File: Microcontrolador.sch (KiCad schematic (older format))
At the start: 16 parts, among them U3 EFM32TG11B120F128GM32, Y1 Crystal, Y2 Crystal

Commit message: Issue #1: Correción de las conexiones Bus
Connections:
- net +3V3: now also C16.1, U3.20 (DVDD)
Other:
- note added: "Conexión UART0 (Location 5)\nU0_CTS: PD5\nU0_RTS: PD6\nU0_RX: PF2\nU0_TX: PF1\n\nComo configurar la funcionalidad de bootloader??\nSegún datasheet está en los pines PF0 y PF1:\nBOOT_RX: PF1\nBOOT_TX: PF0"
- note added: "Requerimientos de Tensión\n==================\n\nVREGVDD = AVDD (Debe ser el mayor volaje del sistema)\nAVDD >= DVDD\nAVDD >= IOVDD"
- note removed: "- PA0\nA: BUSBY BUSAX | LCD_SEG13 \nT: TIM0_CC0 #0 | TIM0_CC1 #7 | PCNT0_S0IN #4\nC: US1_RX #5 | US3_TX #0 | LEU0_RX #4 | I2C0_SDA #0\nO: CMU_CLK2 #0 | PRS_CH0 #0 | PRS_CH3 #3 | GPIO_EM4WU0\n\n- PA1\nA: BUSAY BUSBX | LCD_SEG14\nT: TIM0_CC0 #7 | TIM0_CC1 #0 | PCNT0_S1IN #4\nC: US3_RX #0 | I2C0_SCL #0\nO: CMU_CLK1 #0 PRS_CH1 #0\n\n- PA2\nA: BUSBY BUSAX | LCD_SEG15\nT: TIM0_CC2 #0\nC: US1_RX #6 | US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"
- note removed: "Conexión UART0 (Location 5)\nU0_CTS: PD5\nU0_RTS: PD6\nU0_RX: PF2\nU0_TX: PF1"
- note removed: "TABLA FUNCIONALIDAD GPIOs"
- moved on the sheet: C17, U3A

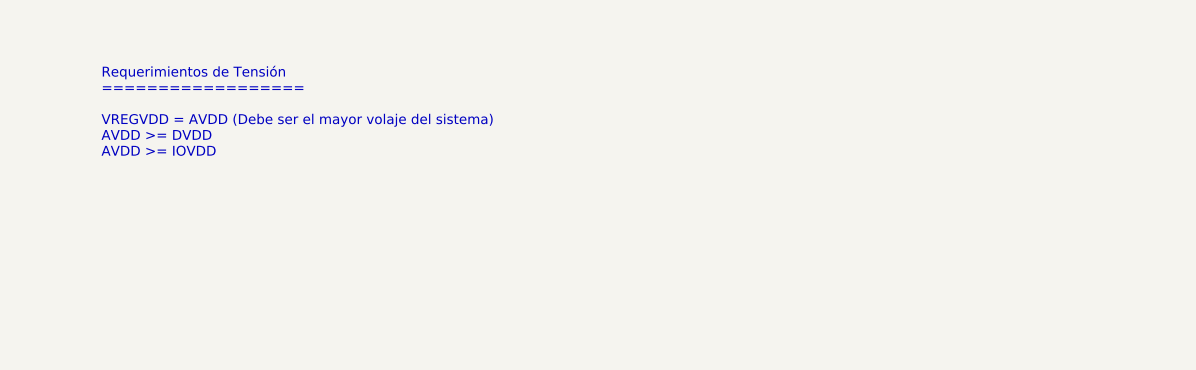
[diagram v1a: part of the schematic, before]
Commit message: Issue #1: Cambio de regulador de voltaje
Se reemplazó el MAX8887 de Maxim por el SP6260 de Maxlinear.
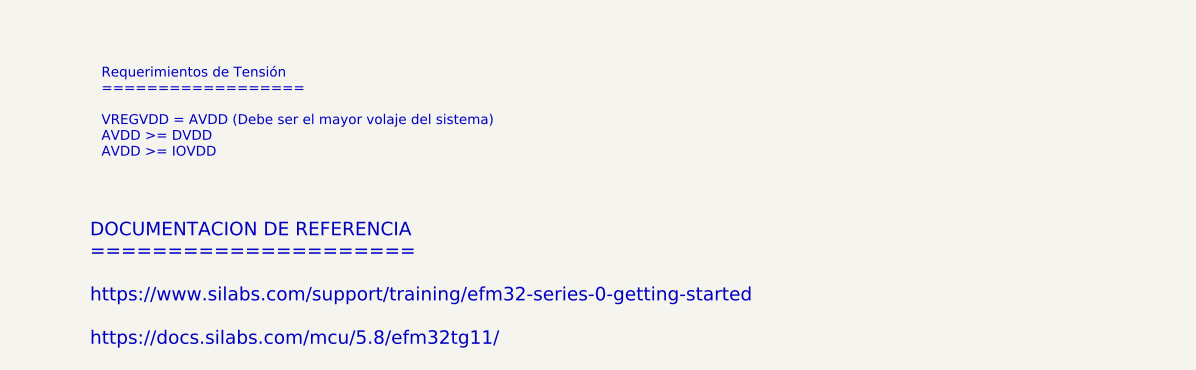
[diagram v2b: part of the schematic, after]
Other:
- note added: "DOCUMENTACION DE REFERENCIA\n=====================\n\nhttps://www.silabs.com/support/training/efm32-series-0-getting-started\n\nhttps://docs.silabs.com/mcu/5.8/efm32tg11/\n"
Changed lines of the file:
@@
 Wire Bus Line
 	6425 3525 6425 4425
+Text Notes 1500 6700 0    59   ~ 0
+DOCUMENTACION DE REFERENCIA\n=====================\n\nhttps://www.silabs.com/support/training/efm32-series-0-getting-started\n\nhttps://docs.silabs.com/mcu/5.8/efm32tg11/\n
 $EndSCHEMATC

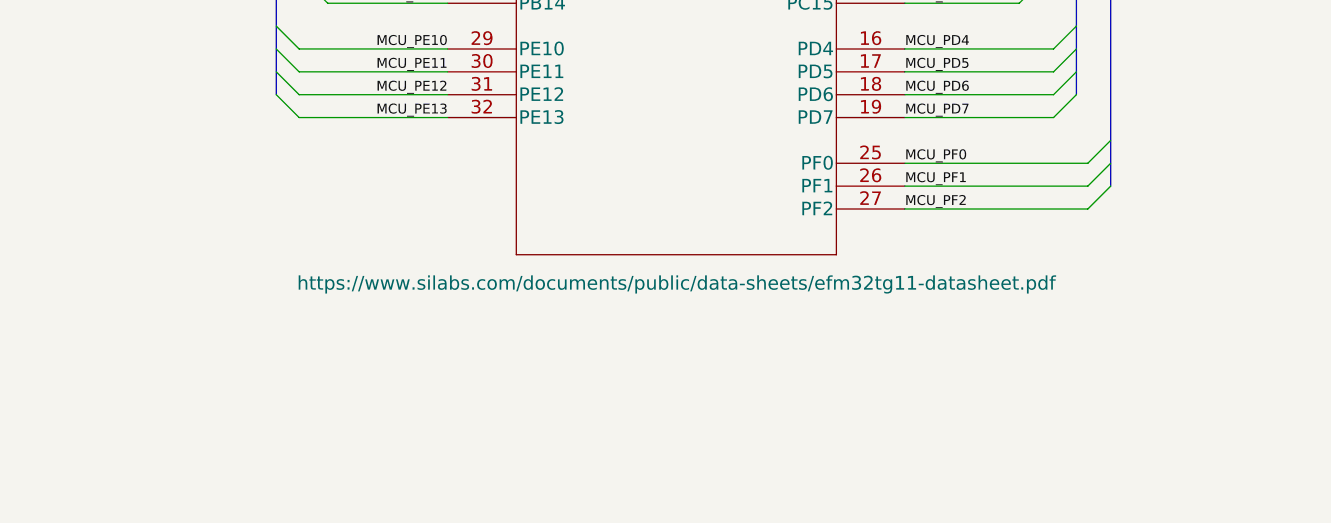
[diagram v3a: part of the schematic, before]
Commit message: Issue #1: Mejora de la funcionalidad de reset
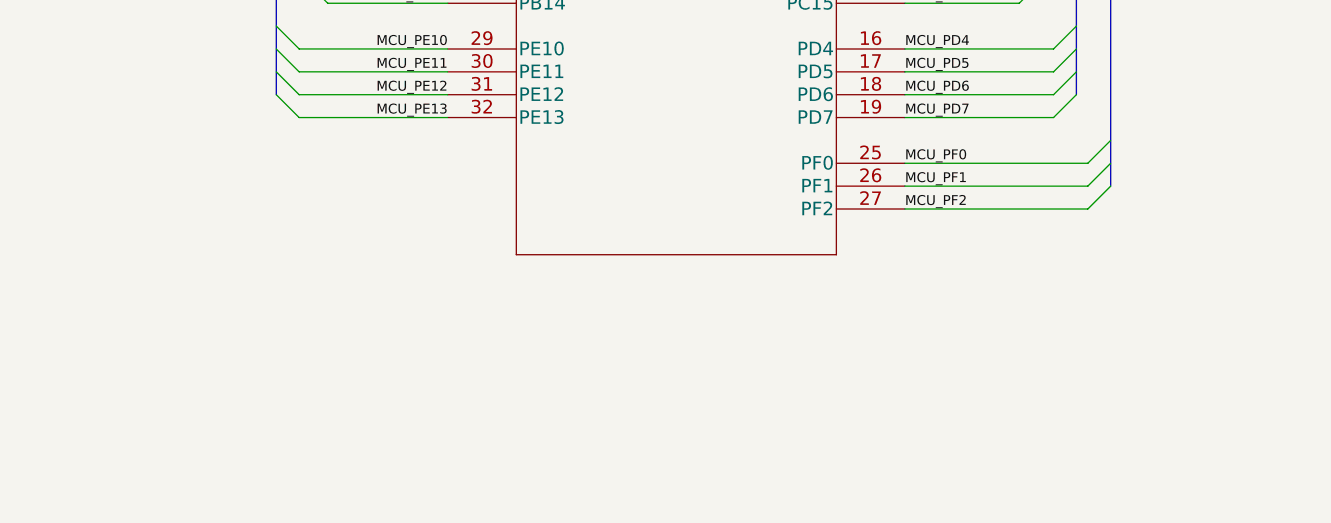
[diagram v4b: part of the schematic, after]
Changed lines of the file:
@@
 F 1 "EFM32TG11B120F128GM32" H 8050 3806 60  0000 C CNN
 F 2 "Mis Huellas:EFM32TG11B120F128GM32" H 8050 3765 60  0001 C CNN
-F 3 "https://www.silabs.com/documents/public/data-sheets/efm32tg11-datasheet.pdf" H 8050 1300 60  0000 C CNN
+F 3 "https://www.silabs.com/documents/public/data-sheets/efm32tg11-datasheet.pdf" H 8050 1300 60  0001 C CNN
 	1    7050 3525
 	1    0    0    -1

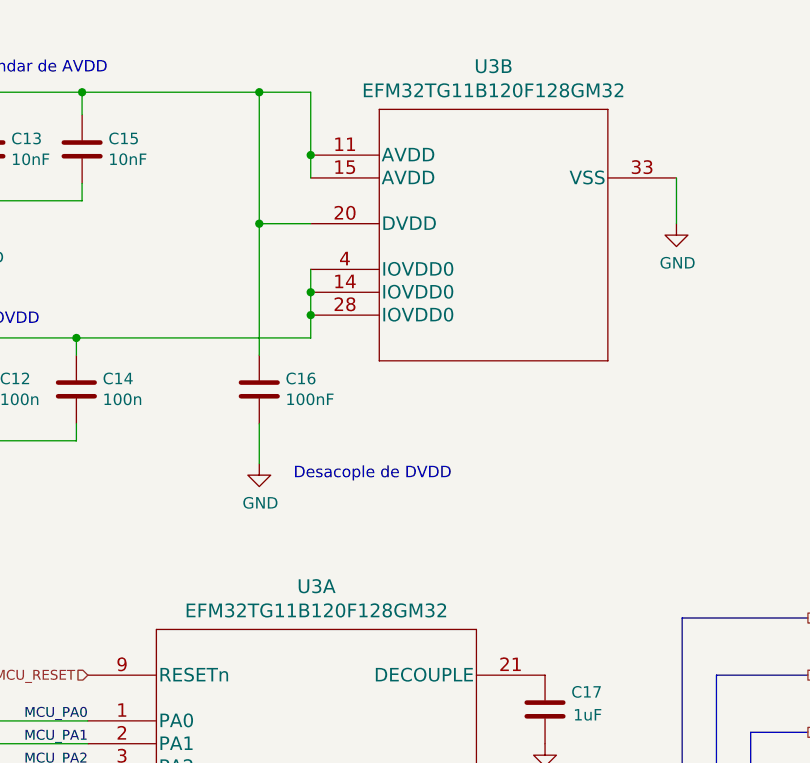
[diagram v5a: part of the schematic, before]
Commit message: Issue #1: Se agregan LEDs para líneas TX/RX de UART
Se agregan los LEDs para indicar comunicación vía UART. Se utilizó un
OpAmp para evitar un consumo excesivo de corriente en las líneas de
comunicación.

Referencia: https://bit.ly/2E7PuVE
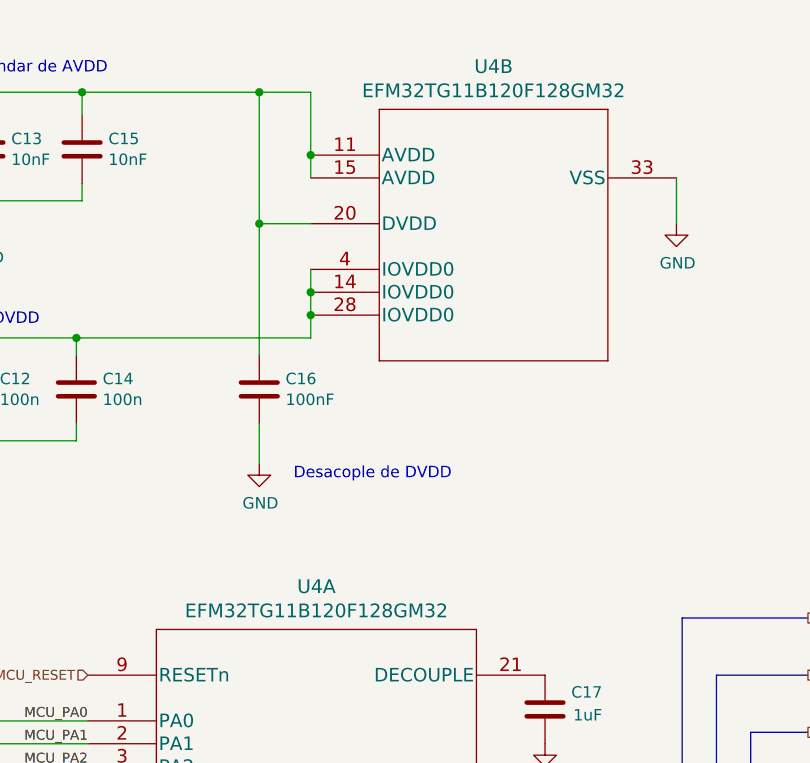
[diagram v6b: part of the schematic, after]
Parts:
- renumbered U3 to U4
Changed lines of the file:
@@
 P 7050 3525
 AR Path="/5F4D785E" Ref="U?"  Part="1"
-AR Path="/5F4D1FFB/5F4D785E" Ref="U3"  Part="1"
-F 0 "U3" H 8050 3912 60  0000 C CNN
+AR Path="/5F4D1FFB/5F4D785E" Ref="U4"  Part="1"
+F 0 "U4" H 8050 3912 60  0000 C CNN
 F 1 "EFM32TG11B120F128GM32" H 8050 3806 60  0000 C CNN
 F 2 "Mis Huellas:EFM32TG11B120F128GM32" H 8050 3765 60  0001 C CNN
@@
 P 8025 1250
 AR Path="/5F4D7864" Ref="U?"  Part="2"
-AR Path="/5F4D1FFB/5F4D7864" Ref="U3"  Part="2"
-F 0 "U3" H 8825 1637 60  0000 C CNN
+AR Path="/5F4D1FFB/5F4D7864" Ref="U4"  Part="2"
+F 0 "U4" H 8825 1637 60  0000 C CNN
 F 1 "EFM32TG11B120F128GM32" H 8825 1531 60  0000 C CNN
 F 2 "Mis Huellas:EFM32TG11B120F128GM32" H 9025 1490 60  0001 C CNN
@@
 P 9625 1550
 AR Path="/5F4D789A" Ref="#PWR?"  Part="1"
-AR Path="/5F4D1FFB/5F4D789A" Ref="#PWR034"  Part="1"
-F 0 "#PWR034" H 9625 1300 50  0001 C CNN
+AR Path="/5F4D1FFB/5F4D789A" Ref="#PWR038"  Part="1"
+F 0 "#PWR038" H 9625 1300 50  0001 C CNN
 F 1 "GND" H 9630 1377 50  0000 C CNN
 F 2 "" H 9625 1550 50  0001 C CNN
@@
 P 7800 2600
 AR Path="/5F4F6C62" Ref="#PWR?"  Part="1"
-AR Path="/5F4D1FFB/5F4F6C62" Ref="#PWR032"  Part="1"
-F 0 "#PWR032" H 7800 2350 50  0001 C CNN
+AR Path="/5F4D1FFB/5F4F6C62" Ref="#PWR036"  Part="1"
+F 0 "#PWR036" H 7800 2350 50  0001 C CNN
 F 1 "GND" H 7805 2427 50  0000 C CNN
 F 2 "" H 7800 2600 50  0001 C CNN
@@
 P 9050 3825
 AR Path="/5F50B022" Ref="#PWR?"  Part="1"
-AR Path="/5F4D1FFB/5F50B022" Ref="#PWR033"  Part="1"
-F 0 "#PWR033" H 9050 3575 50  0001 C CNN
+AR Path="/5F4D1FFB/5F50B022" Ref="#PWR037"  Part="1"
+F 0 "#PWR037" H 9050 3575 50  0001 C CNN
 F 1 "GND" H 9055 3652 50  0000 C CNN
 F 2 "" H 9050 3825 50  0001 C CNN
@@
 P 6600 1525
 AR Path="/5F50B78B" Ref="#PWR?"  Part="1"
-AR Path="/5F4D1FFB/5F50B78B" Ref="#PWR031"  Part="1"
-F 0 "#PWR031" H 6600 1275 50  0001 C CNN
+AR Path="/5F4D1FFB/5F50B78B" Ref="#PWR035"  Part="1"
+F 0 "#PWR035" H 6600 1275 50  0001 C CNN
 F 1 "GND" H 6605 1352 50  0000 C CNN
 F 2 "" H 6600 1525 50  0001 C CNN
@@
 P 2200 2050
 AR Path="/5F50B9C5" Ref="#PWR?"  Part="1"
-AR Path="/5F4D1FFB/5F50B9C5" Ref="#PWR025"  Part="1"
-F 0 "#PWR025" H 2200 1800 50  0001 C CNN
+AR Path="/5F4D1FFB/5F50B9C5" Ref="#PWR029"  Part="1"
+F 0 "#PWR029" H 2200 1800 50  0001 C CNN
 F 1 "GND" H 2205 1877 50  0000 C CNN
 F 2 "" H 2200 2050 50  0001 C CNN
@@
 P 6325 2600
 AR Path="/5F50B4BA" Ref="#PWR?"  Part="1"
-AR Path="/5F4D1FFB/5F50B4BA" Ref="#PWR030"  Part="1"
-F 0 "#PWR030" H 6325 2350 50  0001 C CNN
+AR Path="/5F4D1FFB/5F50B4BA" Ref="#PWR034"  Part="1"
+F 0 "#PWR034" H 6325 2350 50  0001 C CNN
 F 1 "GND" H 6330 2427 50  0000 C CNN
 F 2 "" H 6325 2600 50  0001 C CNN
@@
 	8025 1250 8025 1350
 $Comp
-L power:+3V3 #PWR029
+L power:+3V3 #PWR033
 U 1 1 5F52FE3B
 P 5900 875
-F 0 "#PWR029" H 5900 725 50  0001 C CNN
+F 0 "#PWR033" H 5900 725 50  0001 C CNN
 F 1 "+3V3" H 5915 1048 50  0000 C CNN
 F 2 "" H 5900 875 50  0001 C CNN
@@
 Connection ~ 6200 975
 $Comp
-L power:+3V3 #PWR028
+L power:+3V3 #PWR032
 U 1 1 5F531E0C
 P 5400 1875
-F 0 "#PWR028" H 5400 1725 50  0001 C CNN
+F 0 "#PWR032" H 5400 1725 50  0001 C CNN
 F 1 "+3V3" H 5415 2048 50  0000 C CNN
 F 2 "" H 5400 1875 50  0001 C CNN
@@
 P 1275 2050
 AR Path="/5F543E5C" Ref="#PWR?"  Part="1"
-AR Path="/5F4D1FFB/5F543E5C" Ref="#PWR024"  Part="1"
-F 0 "#PWR024" H 1275 1800 50  0001 C CNN
+AR Path="/5F4D1FFB/5F543E5C" Ref="#PWR028"  Part="1"
+F 0 "#PWR028" H 1275 1800 50  0001 C CNN
 F 1 "GND" H 1280 1877 50  0000 C CNN
 F 2 "" H 1275 2050 50  0001 C CNN
@@
 P 4025 2050
 AR Path="/5F550508" Ref="#PWR?"  Part="1"
-AR Path="/5F4D1FFB/5F550508" Ref="#PWR027"  Part="1"
-F 0 "#PWR027" H 4025 1800 50  0001 C CNN
+AR Path="/5F4D1FFB/5F550508" Ref="#PWR031"  Part="1"
+F 0 "#PWR031" H 4025 1800 50  0001 C CNN
 F 1 "GND" H 4030 1877 50  0000 C CNN
 F 2 "" H 4025 2050 50  0001 C CNN
@@
 P 3100 2050
 AR Path="/5F550512" Ref="#PWR?"  Part="1"
-AR Path="/5F4D1FFB/5F550512" Ref="#PWR026"  Part="1"
-F 0 "#PWR026" H 3100 1800 50  0001 C CNN
+AR Path="/5F4D1FFB/5F550512" Ref="#PWR030"  Part="1"
+F 0 "#PWR030" H 3100 1800 50  0001 C CNN
 F 1 "GND" H 3105 1877 50  0000 C CNN
 F 2 "" H 3100 2050 50  0001 C CNN
